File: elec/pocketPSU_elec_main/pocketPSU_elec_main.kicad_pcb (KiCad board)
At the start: 2 copper layers, 2 parts, among them J1 Conn_01x12_MountingPin, U1 2N7002_C5224215

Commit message: lad into layout
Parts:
- added SW1: EC11E09244BS, footprints:SW-TH_EC11XXXXXXXX, F.Cu at (138.6, 63.8)
- added SW2: TS-1187A-B-A-B, footprints:SW-SMD_4P-L5.1-W5.1-P3.70-LS6.5-TL-2, F.Cu at (117.9, 40.3)
- added SW3: TS-1187A-B-A-B, footprints:SW-SMD_4P-L5.1-W5.1-P3.70-LS6.5-TL-2, F.Cu at (117.9, 46.6)
- added SW4: TS-1187A-B-A-B, footprints:SW-SMD_4P-L5.1-W5.1-P3.70-LS6.5-TL-2, F.Cu at (117.9, 53.0)
- added SW5: TS-1187A-B-A-B, footprints:SW-SMD_4P-L5.1-W5.1-P3.70-LS6.5-TL-2, F.Cu at (117.9, 59.4)
- moved J1 38.2 mm to (95.1, 77.1)
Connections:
- net /user_interface/SPI_CS renamed /SPI_CS
- net /user_interface/SPI_DC renamed /SPI_DC
- net /user_interface/SPI_MOSI renamed /SPI_MOSI
- net /user_interface/SPI_RESET renamed /SPI_RESET
- net /user_interface/SPI_SCK renamed /SPI_SCK

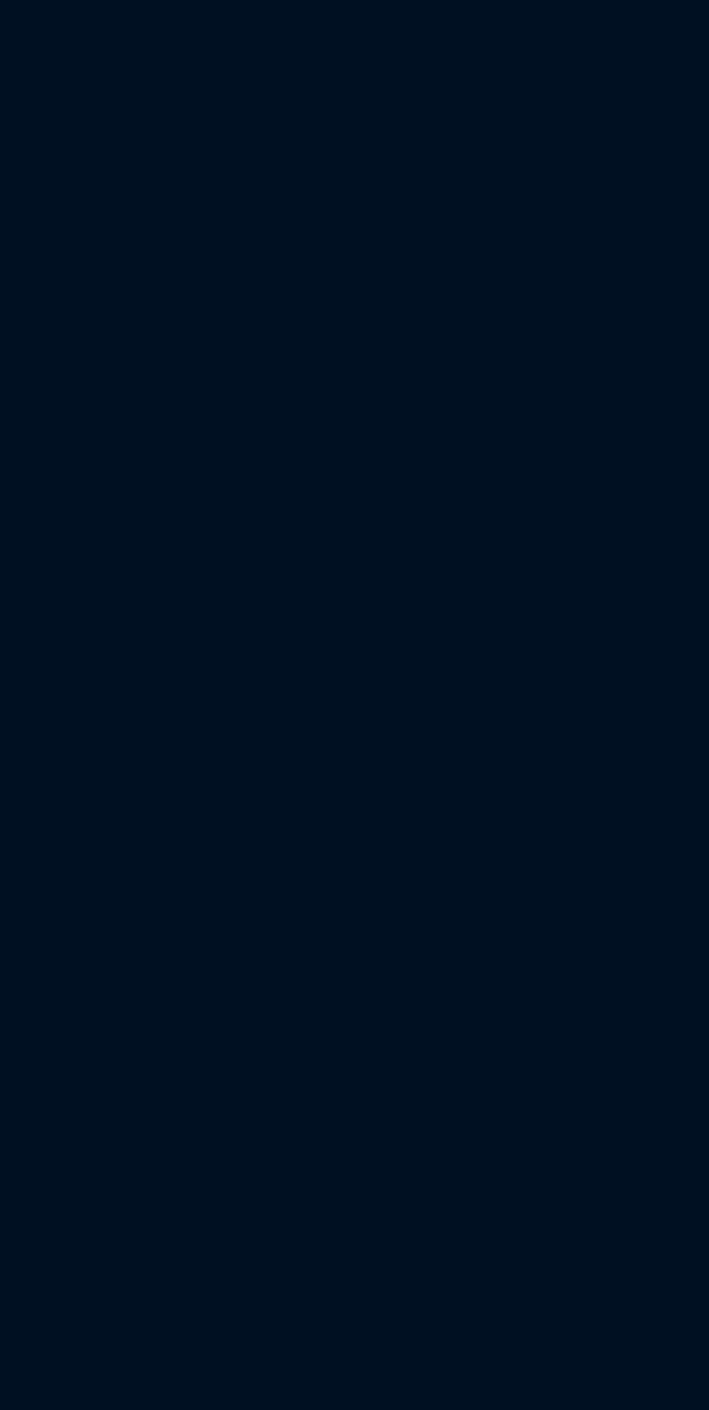
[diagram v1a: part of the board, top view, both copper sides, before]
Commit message: Add footprints, change TFT hookup
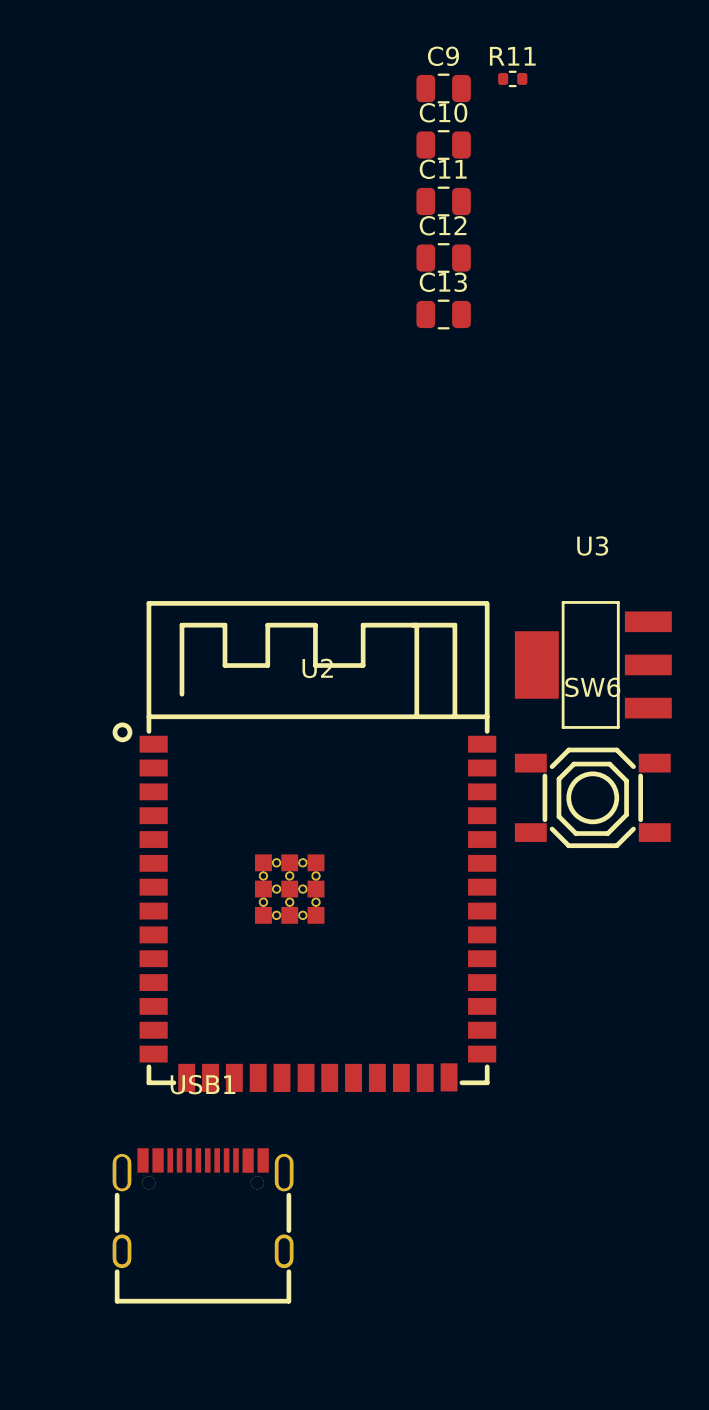
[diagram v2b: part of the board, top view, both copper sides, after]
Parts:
- added C10: 10uF, Capacitor_SMD:C_0805_2012Metric, F.Cu at (181.1, 31.5)
- added C11: 100nF, Capacitor_SMD:C_0805_2012Metric, F.Cu at (181.1, 34.5)
- added C12: 100nF, Capacitor_SMD:C_0805_2012Metric, F.Cu at (181.1, 37.5)
- added C13: 100nF, Capacitor_SMD:C_0805_2012Metric, F.Cu at (181.1, 40.5)
- added C9: 10uF, Capacitor_SMD:C_0805_2012Metric, F.Cu at (181.1, 28.5)
- added R11: 10K, Resistor_SMD:R_0402_1005Metric, F.Cu at (184.7, 27.9)
- added SW6: TS-1187A-B-A-B, footprints:SW-SMD_4P-L5.1-W5.1-P3.70-LS6.5-TL-2, F.Cu at (189.0, 66.2)
- added U2: ESP32-S3-WROOM-1(N16R2), footprints:WIRELM-SMD_ESP32-S3-WROOM-1, F.Cu at (174.3, 72.3)
- added U3: AMS1117-3.3, footprints:SOT-223-3_L6.5-W3.4-P2.30-LS7.0-BR, F.Cu at (189.0, 59.2)
- added USB1: KH-TYPE-C-16P, footprints:USB-C-SMD_KH-TYPE-C-16P, F.Cu at (168.2, 88.0)
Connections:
- net /user_interface/BT_1 renamed /BT_1
- net /user_interface/BT_2 renamed /BT_2
- net /user_interface/BT_3 renamed /BT_3
- net /user_interface/BT_4 renamed /BT_4
- SW1 pad D: /user_interface/ENCODER_BT -> /ENCODER_BT
- U1 pad 1: /user_interface/BACKLIGHT_EN -> /SCREEN_BACKLIGHT_EN

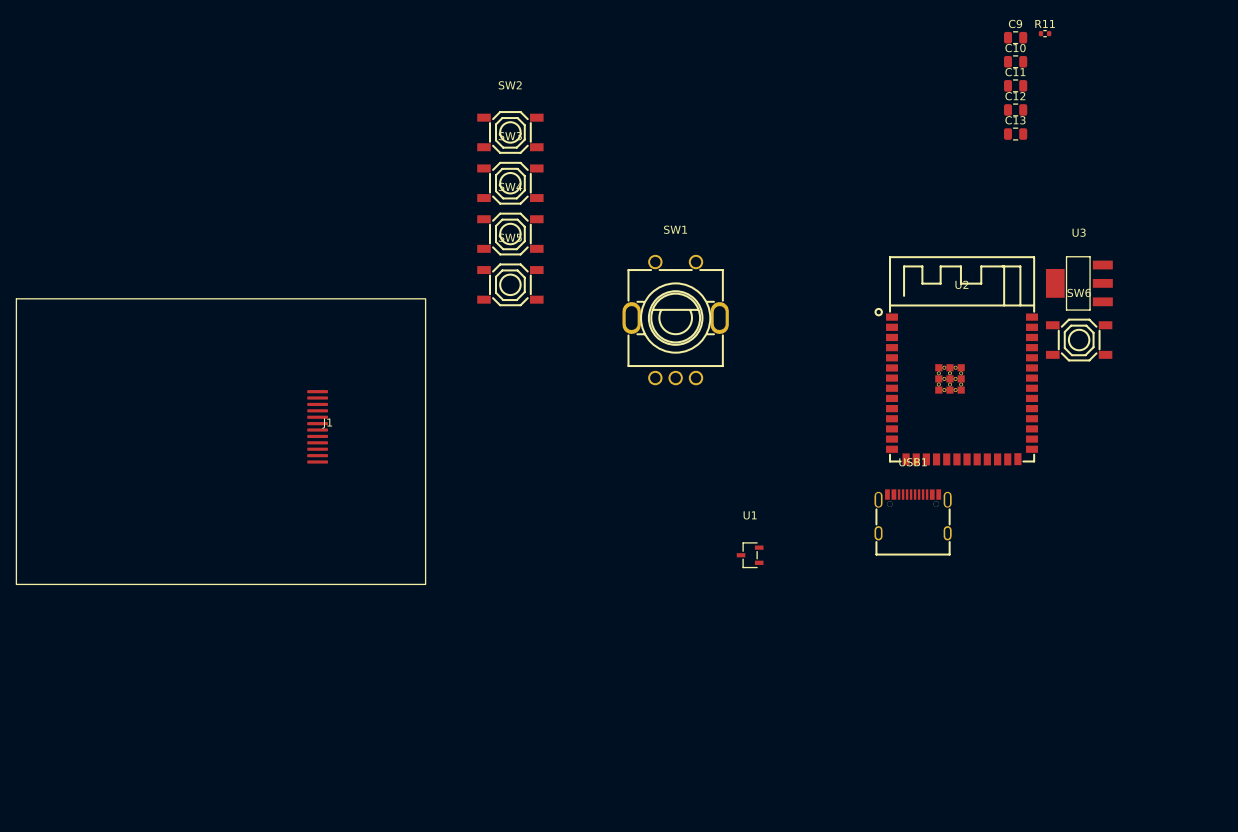
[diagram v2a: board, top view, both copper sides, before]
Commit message: preliminary layout
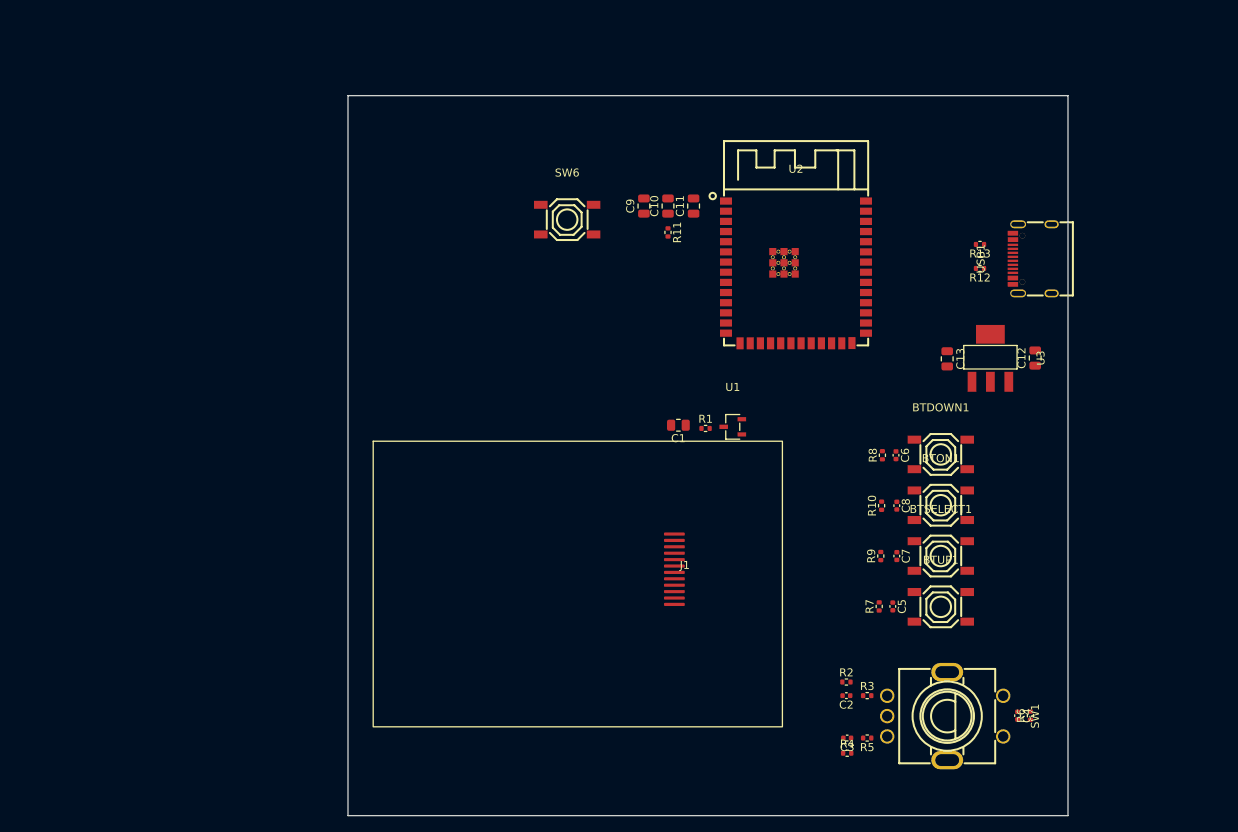
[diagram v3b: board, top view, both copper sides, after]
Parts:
- removed SW2, SW3, SW4, SW5: TS-1187A-B-A-B, footprints:SW-SMD_4P-L5.1-W5.1-P3.70-LS6.5-TL-2
- added BTDOWN1: TS-1187A-B-A-B, footprints:SW-SMD_4P-L5.1-W5.1-P3.70-LS6.5-TL-2, F.Cu at (171.7, 80.5)
- added BTON1: TS-1187A-B-A-B, footprints:SW-SMD_4P-L5.1-W5.1-P3.70-LS6.5-TL-2, F.Cu at (171.7, 86.9)
- added BTSELECT1: TS-1187A-B-A-B, footprints:SW-SMD_4P-L5.1-W5.1-P3.70-LS6.5-TL-2, F.Cu at (171.7, 93.2)
- added BTUP1: TS-1187A-B-A-B, footprints:SW-SMD_4P-L5.1-W5.1-P3.70-LS6.5-TL-2, F.Cu at (171.7, 99.6)
- added C1: 1uF, Resistor_SMD:R_0805_2012Metric, F.Cu at (138.9, 76.9)
- added C2: 10nF, Capacitor_SMD:C_0402_1005Metric, F.Cu at (159.9, 110.7)
- added C3: 10nF, Capacitor_SMD:C_0402_1005Metric, F.Cu at (160.0, 116.0)
- added C4: 10nF, Capacitor_SMD:C_0402_1005Metric, F.Cu at (181.3, 113.2)
- added C5: 10nF, Capacitor_SMD:C_0402_1005Metric, F.Cu at (165.7, 99.5)
- added C6: 10nF, Capacitor_SMD:C_0402_1005Metric, F.Cu at (166.1, 80.7)
- added C7: 10nF, Capacitor_SMD:C_0402_1005Metric, F.Cu at (166.2, 93.2)
- added C8: 10nF, Capacitor_SMD:C_0402_1005Metric, F.Cu at (166.2, 87.0)
- added R1: 4.7R, Resistor_SMD:R_0402_1005Metric, F.Cu at (142.3, 77.3)
- added R10: 10K, Resistor_SMD:R_0402_1005Metric, F.Cu at (164.3, 87.0)
- added R12: 5.1K, Resistor_SMD:R_0402_1005Metric, F.Cu at (176.6, 57.3)
- added R13: 5.1K, Resistor_SMD:R_0402_1005Metric, F.Cu at (176.6, 54.3)
- added R2: 10K, Resistor_SMD:R_0402_1005Metric, F.Cu at (159.9, 109.0)
- added R3: 10K, Resistor_SMD:R_0402_1005Metric, F.Cu at (162.5, 110.7)
- added R4: 10K, Resistor_SMD:R_0402_1005Metric, F.Cu at (160.0, 117.9)
- added R5: 10K, Resistor_SMD:R_0402_1005Metric, F.Cu at (162.5, 116.0)
- added R6: 10K, Resistor_SMD:R_0402_1005Metric, F.Cu at (182.9, 113.2)
- added R7: 10K, Resistor_SMD:R_0402_1005Metric, F.Cu at (164.0, 99.5)
- added R8: 10K, Resistor_SMD:R_0402_1005Metric, F.Cu at (164.4, 80.7)
- added R9: 10K, Resistor_SMD:R_0402_1005Metric, F.Cu at (164.2, 93.2)
- moved SW6 65.7 mm to (125.0, 51.2)
- moved SW1 59.9 mm to (172.2, 113.3), turned to -90 degrees
- moved R11 53.3 mm to (137.6, 52.8), turned to -90 degrees
- moved C9 51.0 mm to (134.6, 49.5), turned to 90 degrees
- moved J1 48.0 mm to (139.7, 94.9)
- moved C10 47.0 mm to (137.6, 49.5), turned to 90 degrees
- moved C11 43.0 mm to (140.8, 49.5), turned to 90 degrees
- moved USB1 35.2 mm to (183.1, 56.1), turned to 90 degrees
- moved C12 31.1 mm to (183.5, 68.5), turned to 90 degrees
- moved C13 29.4 mm to (172.5, 68.6), turned to -90 degrees
- moved U2 25.3 mm to (153.6, 57.8)
- moved U1 16.2 mm to (145.7, 77.1)
- moved U3 14.5 mm to (177.9, 68.5), turned to -90 degrees
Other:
- board outline added: 90 x 90 mm

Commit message: fix caps values, rework layout
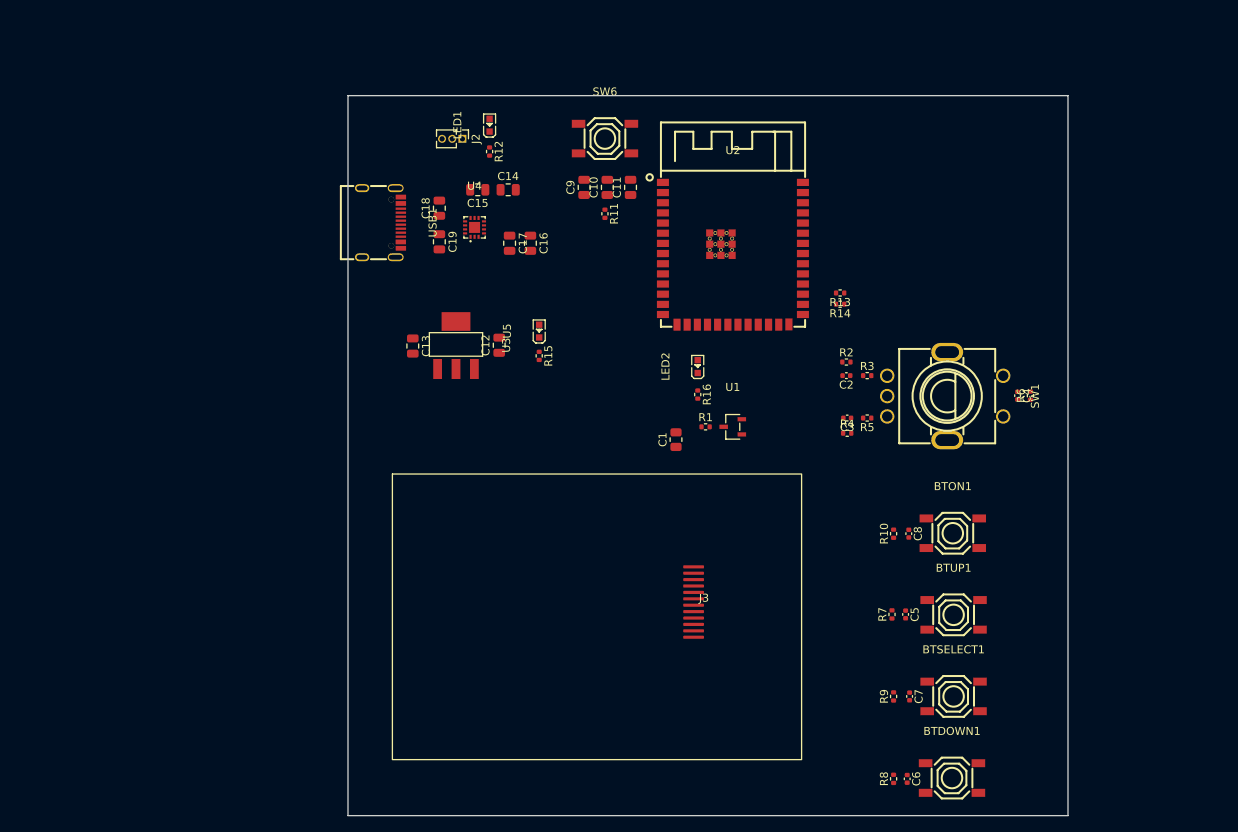
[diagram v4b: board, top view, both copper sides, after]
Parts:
- removed J1: Conn_01x12_MountingPin, footprints:LCD-GMT020-02
- added C14: 10uF, Capacitor_SMD:C_0805_2012Metric, F.Cu at (117.6, 47.5)
- added C15: 100nF, Capacitor_SMD:C_0805_2012Metric, F.Cu at (113.8, 47.5)
- added C16: 1uF, Capacitor_SMD:C_0805_2012Metric, F.Cu at (120.4, 54.1)
- added C17: 100nF, Capacitor_SMD:C_0805_2012Metric, F.Cu at (117.8, 54.1)
- added C18: 300pF, Capacitor_SMD:C_0805_2012Metric, F.Cu at (109.0, 49.8)
- added C19: 300pF, Capacitor_SMD:C_0805_2012Metric, F.Cu at (109.0, 54.0)
- added J2: Conn_01x03_Pin, Connector_PinHeader_1.27mm:PinHeader_1x03_P1.27mm_Vertical, F.Cu at (111.9, 41.1)
- added J3: Conn_01x12_Pin, footprints:LCD-GMT020-02, F.Cu at (142.1, 99.0)
- added LED1: KT-0603R, footprints:LED0603-RD, F.Cu at (115.3, 39.4)
- added LED2: KT-0603R, footprints:LED0603-RD, F.Cu at (141.3, 69.6)
- added R14: 4.7K, Resistor_SMD:R_0402_1005Metric, F.Cu at (159.1, 61.8)
- added R15: 100R, Resistor_SMD:R_0402_1005Metric, F.Cu at (121.5, 68.2)
- added R16: 100R, Resistor_SMD:R_0402_1005Metric, F.Cu at (141.3, 73.1)
- added U4: FUSB302MPX, footprints:MLP-14_L2.5-W2.5-P0.50-BL-EP, F.Cu at (113.4, 52.2)
- added U5: F.0603.00026/P2-0603B1TS2-06T-001, footprints:LED0603-RD, F.Cu at (121.5, 65.1)
- R12: value 5.1K -> 100R
- R13: value 5.1K -> 4.7k
- moved USB1 81.5 mm to (101.8, 51.6), turned to -90 degrees
- moved C12 67.0 mm to (116.5, 66.9)
- moved U3 66.8 mm to (111.1, 66.9)
- moved C13 66.8 mm to (105.7, 67.0)
- moved R12 63.0 mm to (115.3, 42.7), turned to -90 degrees
- moved BTDOWN1 40.5 mm to (173.1, 121.0)
- moved C6 40.5 mm to (167.5, 121.1)
- moved R8 40.5 mm to (165.8, 121.1)
- moved C2 40.0 mm to (159.9, 70.7)
- moved C3 40.0 mm to (160.0, 76.0)
- moved C4 40.0 mm to (181.3, 73.2)
- moved R2 40.0 mm to (159.9, 69.0)
- moved R3 40.0 mm to (162.5, 70.7)
- moved R4 40.0 mm to (160.0, 77.9)
- moved R5 40.0 mm to (162.5, 76.0)
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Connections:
- R12 pad 1: Net-(USB1-CC1) -> Net-(LED1-K)
- R13 pad 1: Net-(USB1-CC2) -> +3.3V
- R13 pad 2: GND -> /USB_SCL
- U2 pad 17: unconnected-(U2-IO9-Pad17) -> /microcontroller/BLINKY_LED
- U2 pad 20: /SPI_MOSI -> /SPI_MISO
- U2 pad 21: /SPI_MISO -> /SPI_MOSI
- U2 pad 28: unconnected-(U2-IO35-Pad28) -> /USB_SDA
- U2 pad 29: unconnected-(U2-IO36-Pad29) -> /USB_SCL
- U2 pad 30: unconnected-(U2-IO37-Pad30) -> /USB_INT_N
- USB1 pad A5: Net-(USB1-CC1) -> /usb_input/USB_CC1
- USB1 pad A6: /usb_input/USB_DP -> /USB_DP
- USB1 pad A7: /usb_input/USB_DM -> /USB_DM
- USB1 pad B5: Net-(USB1-CC2) -> /usb_input/USB_CC2
- USB1 pad B6: /usb_input/USB_DP -> /USB_DP
- USB1 pad B7: /usb_input/USB_DM -> /USB_DM

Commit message: add copper fill
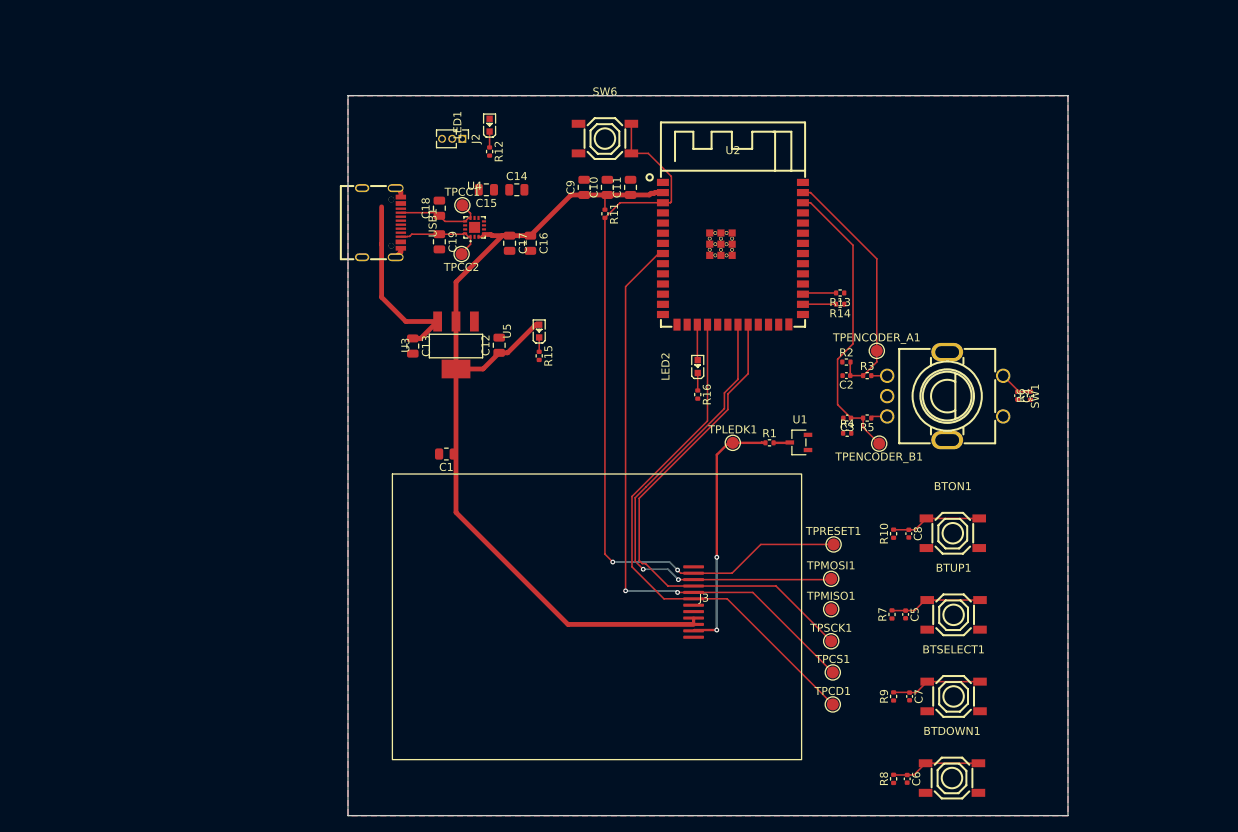
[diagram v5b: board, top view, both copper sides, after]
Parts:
- added TPCC1: TestPoint, TestPoint:TestPoint_Pad_D1.5mm, F.Cu at (111.9, 49.4)
- added TPCC2: TestPoint, TestPoint:TestPoint_Pad_D1.5mm, F.Cu at (111.8, 55.5)
- added TPCD1: TestPoint, TestPoint:TestPoint_Pad_D1.5mm, F.Cu at (158.2, 111.8)
- added TPCS1: TestPoint, TestPoint:TestPoint_Pad_D1.5mm, F.Cu at (158.2, 107.8)
- added TPENCODER_A1: TestPoint, TestPoint:TestPoint_Pad_D1.5mm, F.Cu at (163.7, 67.6)
- added TPENCODER_B1: TestPoint, TestPoint:TestPoint_Pad_D1.5mm, F.Cu at (164.0, 79.2)
- added TPLEDK1: TestPoint, TestPoint:TestPoint_Pad_D1.5mm, F.Cu at (145.7, 79.1)
- added TPMISO1: TestPoint, TestPoint:TestPoint_Pad_D1.5mm, F.Cu at (158.0, 99.9)
- added TPMOSI1: TestPoint, TestPoint:TestPoint_Pad_D1.5mm, F.Cu at (158.0, 96.1)
- added TPRESET1: TestPoint, TestPoint:TestPoint_Pad_D1.5mm, F.Cu at (158.3, 91.8)
- added TPSCK1: TestPoint, TestPoint:TestPoint_Pad_D1.5mm, F.Cu at (158.0, 103.9)
- moved C1 28.8 mm to (109.9, 80.5), turned to 180 degrees
- moved U1 8.50 mm to (154.0, 79.0)
- moved R1 8.24 mm to (150.3, 79.1)
- moved C15 1.08 mm to (114.9, 47.5)
- moved C14 1.08 mm to (118.7, 47.5)
- turned U3 to 90 degrees
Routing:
- net +3.3V: track 0.00 -> 113.4 mm
- net /SPI_RESET: track 0.00 -> 95.3 mm, vias 0 -> 2
- net /SPI_CS: track 0.00 -> 74.5 mm, vias 0 -> 2
- net /SPI_DC: track 0.00 -> 66.4 mm
- net /SPI_SCK: track 0.00 -> 63.3 mm
- net /SPI_MOSI: track 0.00 -> 60.4 mm, vias 0 -> 2
- net /ENCODER_B: track 0.00 -> 37.1 mm
- net /user_interface/LEDK: track 0.00 -> 31.6 mm, vias 0 -> 2
- net /ENCODER_A: track 0.00 -> 31.3 mm
- net VBUS: track 0.00 -> 23.5 mm
- net /usb_input/USB_CC2: track 0.00 -> 11.7 mm
- net /BT_1: track 0.00 -> 11.6 mm
- net /BT_3: track 0.00 -> 11.4 mm
- net /usb_input/USB_CC1: track 0.00 -> 11.4 mm
- net /BT_4: track 0.00 -> 11.3 mm
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- added copper zone on B.Cu, net GND
- added copper zone on F.Cu, net GND
